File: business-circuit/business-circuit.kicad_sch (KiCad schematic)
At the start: 6 parts, among them U1 NT3H2111W0FHKH

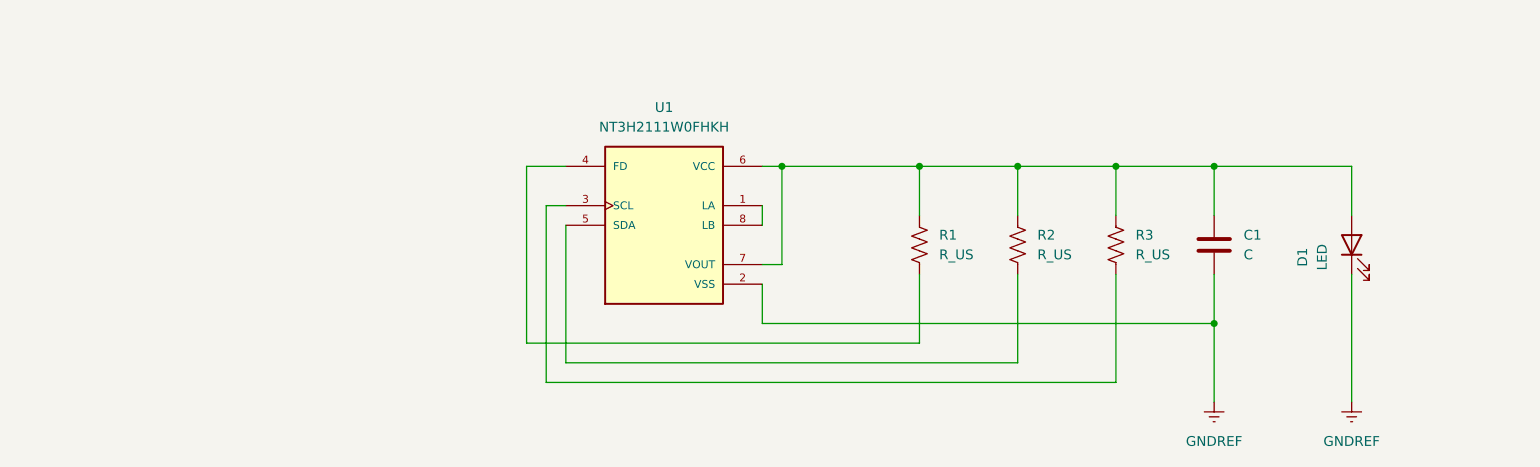
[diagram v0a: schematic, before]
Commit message: schematic done pending clean up
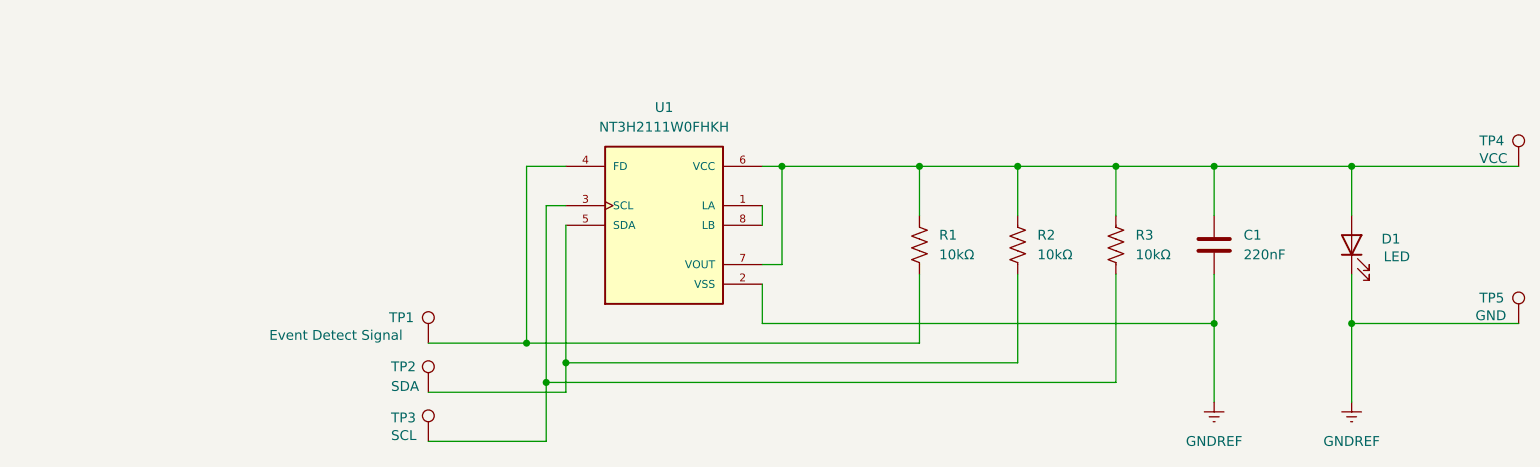
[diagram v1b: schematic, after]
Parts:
- added TP1: Event Detect Signal, TestPoint:TestPoint_Pad_D2.0mm, symbol Connector:TestPoint
- added TP2: SDA, TestPoint:TestPoint_Pad_D2.0mm, symbol Connector:TestPoint
- added TP3: SCL, TestPoint:TestPoint_Pad_D2.0mm, symbol Connector:TestPoint
- added TP4: VCC, TestPoint:TestPoint_Pad_D2.0mm, symbol Connector:TestPoint
- added TP5: GND, TestPoint:TestPoint_Pad_D2.0mm, symbol Connector:TestPoint
- C1: value C -> 220nF; footprint (none) -> Capacitor_SMD:C_0402_1005Metric
- D1: footprint (none) -> LED_SMD:LED_0402_1005Metric
- R1, R2, R3: value R_US -> 10kΩ; footprint (none) -> Resistor_SMD:R_0402_1005Metric
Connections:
- net GNDREF: now also TP5.1
- net at C1.1, D1.2 (A), R1.1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: now also TP4.1
- net at R3.2, U1.3 (SCL): now also TP3.1
- net at R1.2, U1.4 (FD): now also TP1.1
- net at R2.2, U1.5 (SDA): now also TP2.1

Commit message: pre board review
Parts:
- TP1, TP2, TP3, TP4, TP5: footprint TestPoint:TestPoint_Pad_D2.0mm -> TestPoint:TestPoint_Pad_1.0x1.0mm
- U1: footprint NT3H2111W0FHKH:QFN8P50_160X160X50L40X20N -> Library:SOT96-1
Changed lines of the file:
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@@
 			)
 		)
-		(property "Footprint" "TestPoint:TestPoint_Pad_D2.0mm"
+		(property "Footprint" "TestPoint:TestPoint_Pad_1.0x1.0mm"
 			(at 222.25 73.66 0)
 			(effects
@@
 			)
 		)
-		(property "Footprint" "NT3H2111W0FHKH:QFN8P50_160X160X50L40X20N"
+		(property "Footprint" "Library:SOT96-1"
 			(at 107.188 46.482 0)
 			(effects
@@
 			)
 		)
-		(property "Footprint" "TestPoint:TestPoint_Pad_D2.0mm"
+		(property "Footprint" "TestPoint:TestPoint_Pad_1.0x1.0mm"
 			(at 81.28 82.55 0)
 			(effects
@@
 			)
 		)
-		(property "Footprint" "TestPoint:TestPoint_Pad_D2.0mm"
+		(property "Footprint" "TestPoint:TestPoint_Pad_1.0x1.0mm"
 			(at 81.28 76.2 0)
 			(effects
@@
 			)
 		)
-		(property "Footprint" "TestPoint:TestPoint_Pad_D2.0mm"
+		(property "Footprint" "TestPoint:TestPoint_Pad_1.0x1.0mm"
 			(at 81.28 88.9 0)
 			(effects
@@
 			)
 		)
-		(property "Footprint" "TestPoint:TestPoint_Pad_D2.0mm"
+		(property "Footprint" "TestPoint:TestPoint_Pad_1.0x1.0mm"
 			(at 222.25 53.34 0)
 			(effects

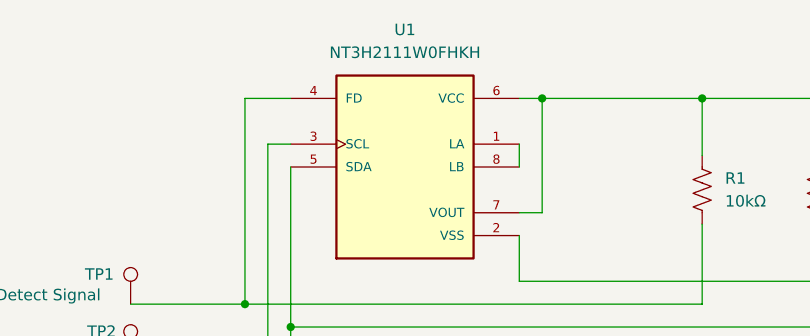
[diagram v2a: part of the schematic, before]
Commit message: need to add antenna
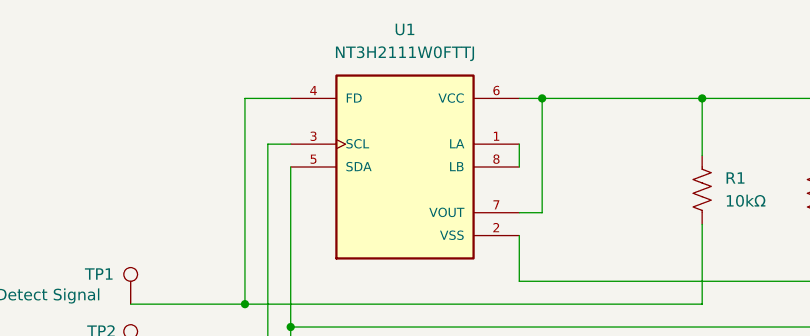
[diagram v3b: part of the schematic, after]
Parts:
- U1: value NT3H2111W0FHKH -> NT3H2111W0FTTJ
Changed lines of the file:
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@@
 			)
 		)
-		(property "Value" "NT3H2111W0FHKH"
+		(property "Value" "NT3H2111W0FTTJ"
 			(at 106.68 48.26 0)
 			(effects
@@
 			)
 		)
-		(property "Datasheet" ""
+		(property "Datasheet" "https://www.nxp.com/docs/en/data-sheet/NT3H2111_2211.pdf"
 			(at 106.68 60.96 0)
 			(effects
@@
 			)
 		)
-		(property "Description" ""
+		(property "Description" "IC RFID TRANSP 13.56MHZ 8TSSOP"
 			(at 106.68 60.96 0)
 			(effects

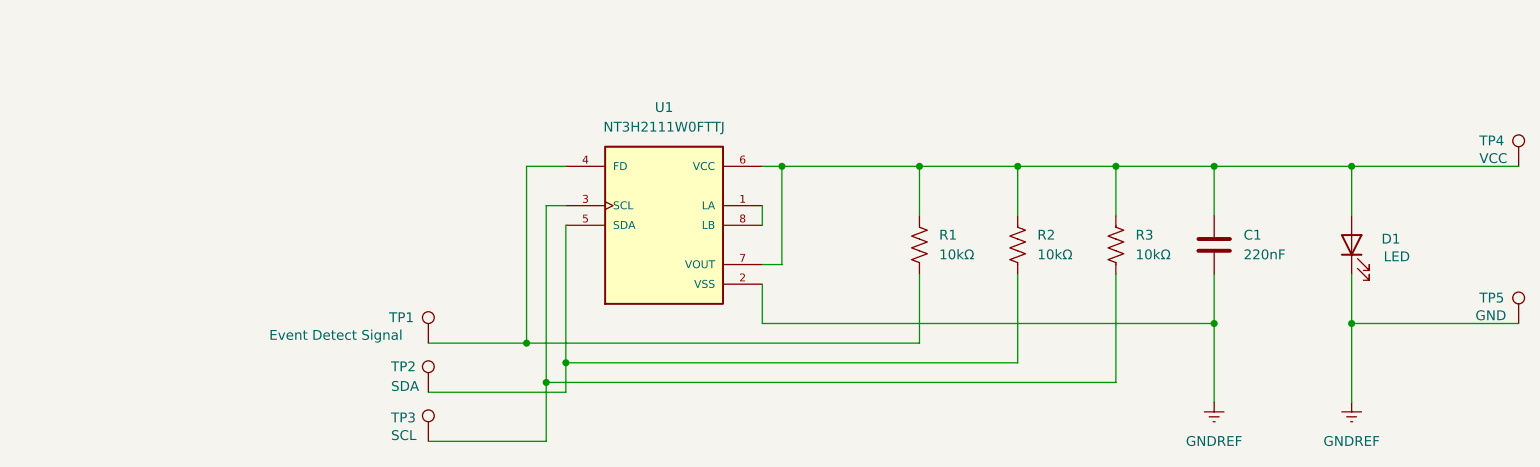
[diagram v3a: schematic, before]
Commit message: redid schematic with antenna
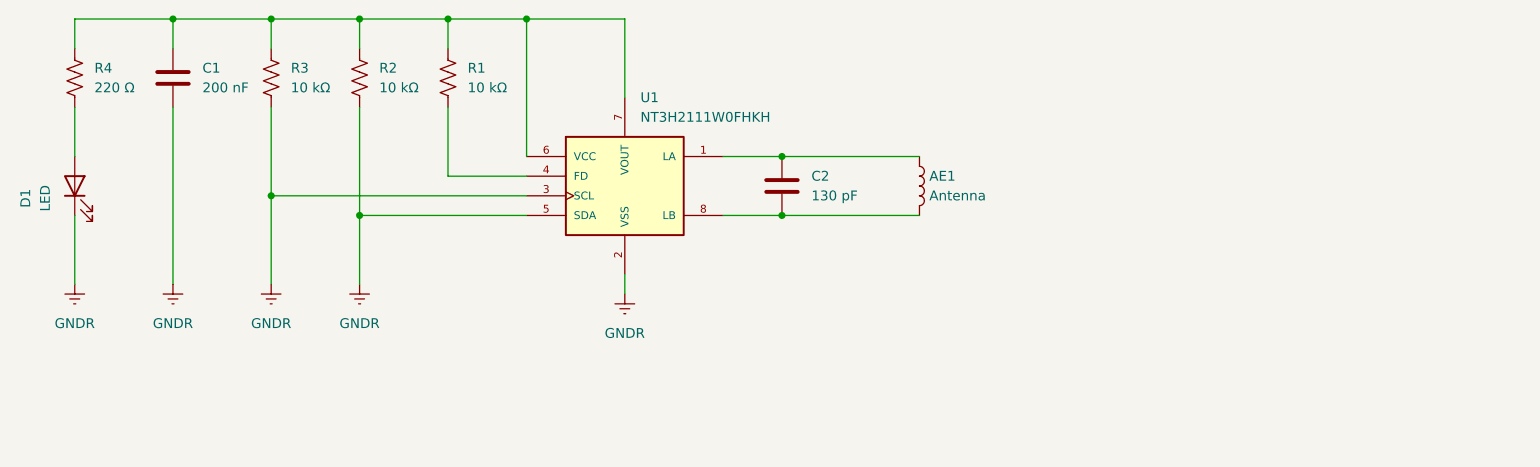
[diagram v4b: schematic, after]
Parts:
- removed TP1: Event Detect Signal, TestPoint:TestPoint_Pad_1.0x1.0mm, symbol Connector:TestPoint
- removed TP2: SDA, TestPoint:TestPoint_Pad_1.0x1.0mm, symbol Connector:TestPoint
- removed TP3: SCL, TestPoint:TestPoint_Pad_1.0x1.0mm, symbol Connector:TestPoint
- removed TP4: VCC, TestPoint:TestPoint_Pad_1.0x1.0mm, symbol Connector:TestPoint
- removed TP5: GND, TestPoint:TestPoint_Pad_1.0x1.0mm, symbol Connector:TestPoint
- added AE1: Antenna, symbol Device:L
- added C2: 130 pF, Capacitor_SMD:C_0402_1005Metric_Pad0.74x0.62mm_HandSolder, symbol Device:C
- added R4: 220 Ω, Resistor_SMD:R_0402_1005Metric_Pad0.72x0.64mm_HandSolder, symbol Device:R_US
- C1: value 220nF -> 200 nF; footprint Capacitor_SMD:C_0402_1005Metric -> Capacitor_SMD:C_0402_1005Metric_Pad0.74x0.62mm_HandSolder
- D1: footprint LED_SMD:LED_0402_1005Metric -> (none)
- R1, R2, R3: value 10kΩ -> 10 kΩ; footprint Resistor_SMD:R_0402_1005Metric -> Resistor_SMD:R_0402_1005Metric_Pad0.72x0.64mm_HandSolder
- U1: value NT3H2111W0FTTJ -> NT3H2111W0FHKH
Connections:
- net GNDREF is gone; now on net GNDR: C1.2, D1.1 (K), U1.2 (VSS)
- net at C1.1, R1.1, R2.1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: now also R4.1; no longer D1.2 (A)
- net at U1.1 (LA): now also AE1.1, C2.1; no longer U1.8 (LB)
- net GNDR: now reaches R3.2, U1.3 (SCL)
- net GNDR: now also R2.2, U1.5 (SDA)
- new net: AE1.2, C2.2, U1.8 (LB)
- new net: D1.2 (A), R4.2

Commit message: pre importing antenna
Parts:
- AE1: now left out of the parts list
- D1: footprint (none) -> LED_SMD:LED_0402_1005Metric
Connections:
- net GNDR: no longer R2.2, R3.2, U1.3 (SCL), U1.5 (SDA)
- net at AE1.1, C2.1, U1.1 (LA): now also AE1.2, C2.2, U1.8 (LB)
- new net: R3.2, U1.3 (SCL)
- new net: R2.2, U1.5 (SDA)
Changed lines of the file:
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@@
-	)
-	(junction
-		(at 55.88 57.15)
-		(diameter 0)
-		(color 0 0 0 0)
 	)
 	(junction
@@
 	)
 	(junction
-		(at 67.31 59.69)
-		(diameter 0)
-		(color 0 0 0 0)
-	)
-	(junction
 		(at 67.31 34.29)
 		(diameter 0)
@@
 	)
 	(junction
+		(at 138.43 59.69)
+		(diameter 0)
+		(color 0 0 0 0)
+	)
+	(junction
+		(at 138.43 52.07)
+		(diameter 0)
+		(color 0 0 0 0)
+	)
+	(junction
 		(at 121.92 59.69)
 		(diameter 0)
@@
 	(wire
 		(pts
+			(xy 138.43 52.07) (xy 139.7 52.07)
+		)
+		(stroke
+			(width 0)
+			(type default)
+		)
+	)
+	(wire
+		(pts
 			(xy 43.18 34.29) (xy 43.18 38.1)
 		)
@@
 	(wire
 		(pts
-			(xy 55.88 68.58) (xy 55.88 57.15)
-		)
-		(stroke
-			(width 0)
-			(type default)
-		)
-	)
-	(wire
-		(pts
 			(xy 67.31 34.29) (xy 78.74 34.29)
 		)
@@
 	(wire
 		(pts
-			(xy 121.92 52.07) (xy 139.7 52.07)
+			(xy 138.43 59.69) (xy 139.7 59.69)
+		)
+		(stroke
+			(width 0)
+			(type default)
+		)
+	)
+	(wire
+		(pts
+			(xy 121.92 52.07) (xy 138.43 52.07)
 		)
 		(stroke
@@
 	(wire
 		(pts
-			(xy 121.92 59.69) (xy 139.7 59.69)
+			(xy 121.92 59.69) (xy 138.43 59.69)
+		)
+		(stroke
+			(width 0)
+			(type default)
+		)
+	)
+	(wire
+		(pts
+			(xy 138.43 52.07) (xy 138.43 59.69)
 		)
 		(stroke
@@
 		(pts
 			(xy 30.48 59.69) (xy 30.48 68.58)
-		)
-		(stroke
-			(width 0)
-			(type default)
-		)
-	)
-	(wire
-		(pts
-			(xy 67.31 59.69) (xy 67.31 68.58)
 		)
 		(stroke
@@
 		(unit 1)
 		(exclude_from_sim no)
-		(in_bom yes)
-		(on_board yes)
+		(in_bom no)
+		(on_board no)
 		(dnp no)
-		(fields_autoplaced yes)
 		(property "Reference" "AE1"
 			(at 140.97 54.6099 0)
@@
 				(path "/24be31f7-ad2a-4a22-a1db-8a169e926191"
 					(reference "AE1")
-					(unit 1)
-				)
-			)
-		)
-	)
-	(symbol
-		(lib_id "power:GNDREF")
-		(at 67.31 68.58 0)
-		(unit 1)
-		(exclude_from_sim no)
-		(in_bom yes)
-		(on_board yes)
-		(dnp no)
-		(fields_autoplaced yes)
-		(property "Reference" "#PWR04"
-			(at 67.31 74.93 0)
-			(effects
-				(font
-					(size 1.27 1.27)
-				)
-				(hide yes)
-			)
-		)
-		(property "Value" "GNDR"
-			(at 67.31 73.66 0)
-			(effects
-				(font
-					(size 1.27 1.27)
-				)
-			)
-		)
-		(property "Footprint" ""
-			(at 67.31 68.58 0)
-			(effects
-				(font
-					(size 1.27 1.27)
-				)
-				(hide yes)
-			)
-		)
-		(property "Datasheet" ""
-			(at 67.31 68.58 0)
-			(effects
-				(font
-					(size 1.27 1.27)
-				)
-				(hide yes)
-			)
-		)
-		(property "Description" "Power symbol creates a global label with name \"GNDREF\" , reference supply ground"
-			(at 67.31 68.58 0)
-			(effects
-				(font
-					(size 1.27 1.27)
-				)
-				(hide yes)
-			)
-		)
-		(pin "1"
-		)
-		(instances
-			(project "business-circuit"
-				(path "/24be31f7-ad2a-4a22-a1db-8a169e926191"
-					(reference "#PWR04")
 					(unit 1)
 				)
@@
 			)
 		)
-		(property "Footprint" ""
+		(property "Footprint" "LED_SMD:LED_0402_1005Metric"
 			(at 30.48 55.88 0)
 			(effects
@@
 					(unit 1)
 				)
-			)
-		)
-	)
-	(symbol
-		(lib_id "power:GNDREF")
-		(at 55.88 68.58 0)
-		(unit 1)
-		(exclude_from_sim no)
-		(in_bom yes)
-		(on_board yes)
-		(dnp no)
-		(fields_autoplaced yes)
-		(property "Reference" "#PWR03"
-			(at 55.88 74.93 0)
-			(effects
-				(font
-					(size 1.27 1.27)
-				)
-				(hide yes)
-			)
-		)
-		(property "Value" "GNDR"
-			(at 55.88 73.66 0)
-			(effects
-				(font
-					(size 1.27 1.27)
-				)
-			)
-		)
-		(property "Footprint" ""
-			(at 55.88 68.58 0)
-			(effects
-				(font
-					(size 1.27 1.27)
-				)
-				(hide yes)
-			)
-		)
-		(property "Datasheet" ""
-			(at 55.88 68.58 0)
-			(effects
-				(font
-					(size 1.27 1.27)
-				)
-				(hide yes)
-			)
-		)
-		(property "Description" "Power symbol creates a global label with name \"GNDREF\" , reference supply ground"
-			(at 55.88 68.58 0)
-			(effects
-				(font
-					(size 1.27 1.27)
-				)
-				(hide yes)
-			)
-		)
-		(pin "1"
-		)
-		(instances
-			(project "business-circuit"
-				(path "/24be31f7-ad2a-4a22-a1db-8a169e926191"
-					(reference "#PWR03")
-					(unit 1)
-				)

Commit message: antenna broke SRC :(
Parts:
- AE1: footprint (none) -> Library:54X27_3TURNS_THIN
- renumbered R4 to R1, R3 to R2, R2 to R3, R1 to R4
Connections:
- net at AE1.1, C2.1, U1.1 (LA): no longer AE1.2, C2.2, U1.8 (LB)
- new net: AE1.2, C2.2, U1.8 (LB)
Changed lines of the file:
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@@
-	)
-	(junction
-		(at 138.43 59.69)
-		(diameter 0)
-		(color 0 0 0 0)
-	)
-	(junction
-		(at 138.43 52.07)
-		(diameter 0)
-		(color 0 0 0 0)
 	)
 	(junction
@@
 	(wire
 		(pts
-			(xy 138.43 52.07) (xy 139.7 52.07)
+			(xy 121.92 52.07) (xy 139.7 52.07)
 		)
 		(stroke
@@
 	(wire
 		(pts
-			(xy 138.43 59.69) (xy 139.7 59.69)
-		)
-		(stroke
-			(width 0)
-			(type default)
-		)
-	)
-	(wire
-		(pts
-			(xy 121.92 52.07) (xy 138.43 52.07)
+			(xy 121.92 59.69) (xy 139.7 59.69)
 		)
 		(stroke
@@
 		(pts
 			(xy 114.3 59.69) (xy 121.92 59.69)
-		)
-		(stroke
-			(width 0)
-			(type default)
-		)
-	)
-	(wire
-		(pts
-			(xy 121.92 59.69) (xy 138.43 59.69)
-		)
-		(stroke
-			(width 0)
-			(type default)
-		)
-	)
-	(wire
-		(pts
-			(xy 138.43 52.07) (xy 138.43 59.69)
 		)
 		(stroke
@@
 		(exclude_from_sim no)
 		(in_bom no)
-		(on_board no)
+		(on_board yes)
 		(dnp no)
 		(property "Reference" "AE1"
@@
 			)
 		)
-		(property "Footprint" ""
+		(property "Footprint" "Library:54X27_3TURNS_THIN"
 			(at 139.7 55.88 0)
 			(effects
@@
 		(dnp no)
 		(fields_autoplaced yes)
-		(property "Reference" "#PWR01"
+		(property "Reference" "#PWR0102"
 			(at 30.48 74.93 0)
 			(effects
@@
 			(project ""
 				(path "/24be31f7-ad2a-4a22-a1db-8a169e926191"
-					(reference "#PWR01")
+					(reference "#PWR0102")
 					(unit 1)
 				)
@@
 		(on_board yes)
 		(dnp no)
-		(property "Reference" "#PWR05"
+		(property "Reference" "#PWR0101"
 			(at 101.6 76.2 0)
 			(effects
@@
 			(project "business-circuit"
 				(path "/24be31f7-ad2a-4a22-a1db-8a169e926191"
-					(reference "#PWR05")
+					(reference "#PWR0101")
 					(unit 1)
 				)
@@
 		(dnp no)
 		(fields_autoplaced yes)
-		(property "Reference" "R2"
+		(property "Reference" "R3"
 			(at 69.85 40.6399 0)
 			(effects
@@
 			(project "business-circuit"
 				(path "/24be31f7-ad2a-4a22-a1db-8a169e926191"
-					(reference "R2")
+					(reference "R3")
 					(unit 1)
 				)
@@
 		(dnp no)
 		(fields_autoplaced yes)
-		(property "Reference" "R3"
+		(property "Reference" "R2"
 			(at 58.42 40.6399 0)
 			(effects
@@
 			(project "business-circuit"
 				(path "/24be31f7-ad2a-4a22-a1db-8a169e926191"
-					(reference "R3")
+					(reference "R2")
 					(unit 1)
 				)
@@
 		(dnp no)
 		(fields_autoplaced yes)
-		(property "Reference" "R1"
+		(property "Reference" "R4"
 			(at 81.28 40.6399 0)
 			(effects
@@
 			(project ""
 				(path "/24be31f7-ad2a-4a22-a1db-8a169e926191"
-					(reference "R1")
+					(reference "R4")
 					(unit 1)
 				)
@@
 		(dnp no)
 		(fields_autoplaced yes)
-		(property "Reference" "R4"
+		(property "Reference" "R1"
 			(at 33.02 40.6399 0)
 			(effects
@@
 			(project "business-circuit"
 				(path "/24be31f7-ad2a-4a22-a1db-8a169e926191"
-					(reference "R4")
+					(reference "R1")
 					(unit 1)
 				)
@@
 		(dnp no)
 		(fields_autoplaced yes)
-		(property "Reference" "#PWR02"
+		(property "Reference" "#PWR0103"
 			(at 43.18 74.93 0)
 			(effects
@@
 			(project "business-circuit"
 				(path "/24be31f7-ad2a-4a22-a1db-8a169e926191"
-					(reference "#PWR02")
-					(unit 1)
-				)
+					(reference "#PWR0103")
+					(unit 1)
+				)
